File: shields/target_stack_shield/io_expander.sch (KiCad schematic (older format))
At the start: 8 parts

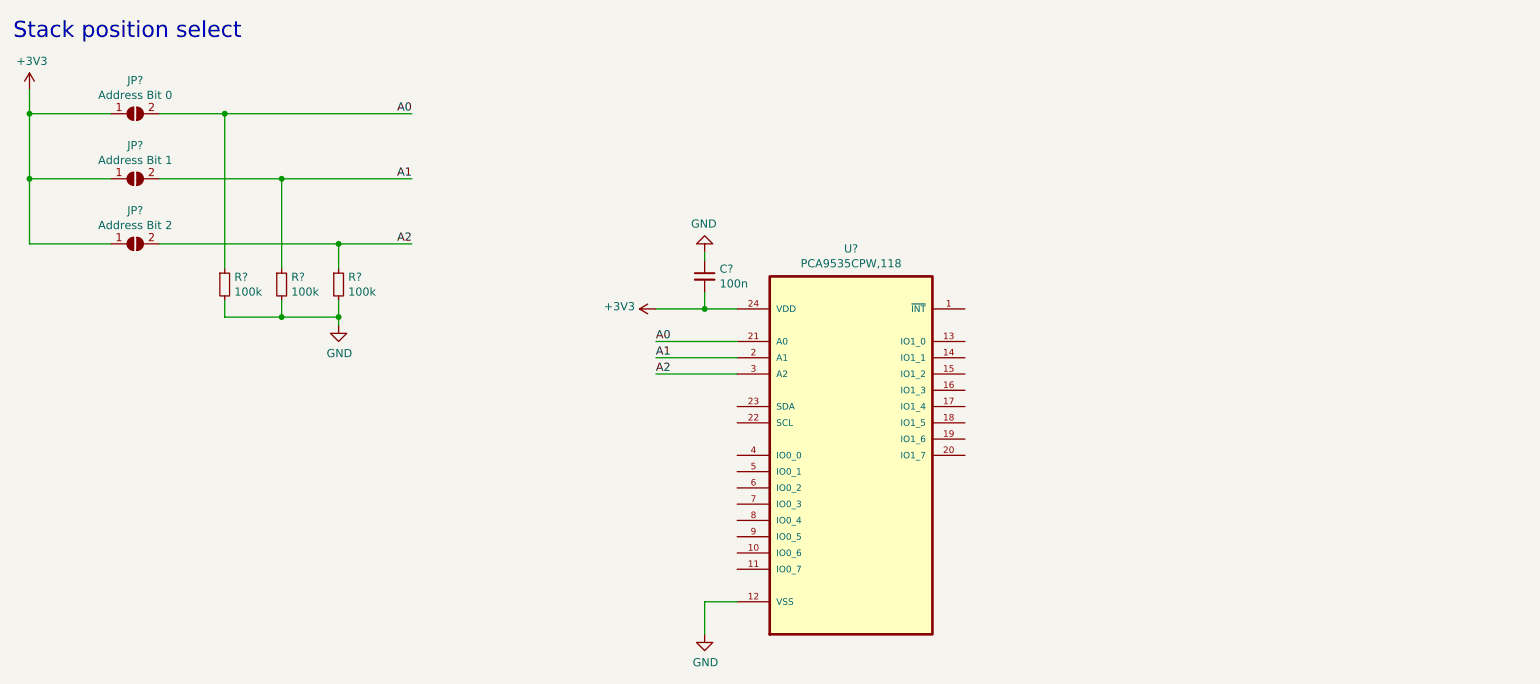
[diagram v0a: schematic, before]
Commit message: further work on target stack shield schematics
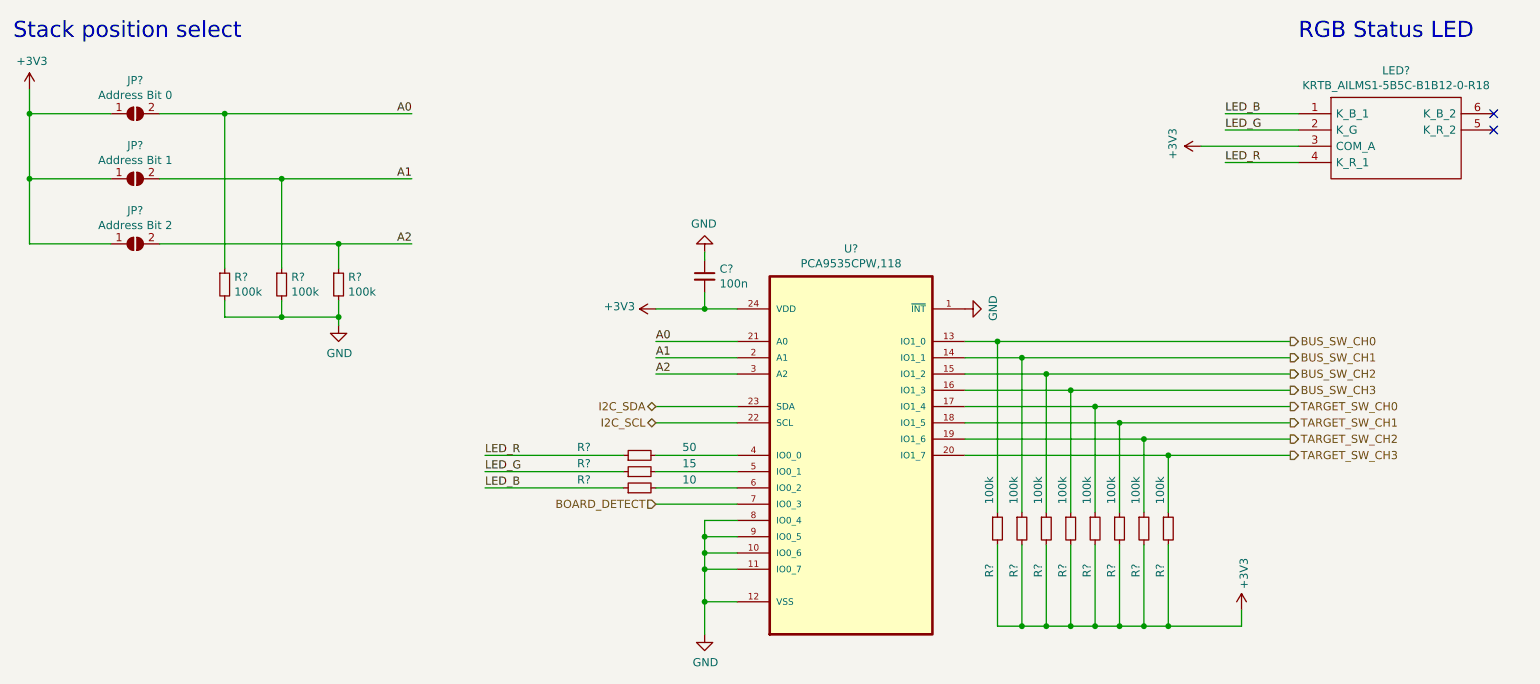
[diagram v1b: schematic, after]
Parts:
- added LED?: KRTB_AILMS1-5B5C-B1B12-0-R18, KRTBAILMS15B5CB1B120R18, symbol hive:KRTB_AILMS1-5B5C-B1B12-0-R18
- added R?: 50, symbol Device:R_Small
- added R?: 15, symbol Device:R_Small
- added R?: 10, symbol Device:R_Small
- added R? (x8): 100k, symbol Device:R_Small
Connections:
- net +3V3: now also LED?.3 (COM_A), R?.2, R?.2, R?.2, R?.2, R?.2, R?.2, R?.2, R?.2
- net GND: now also U?.1 (~INT), U?.10 (IO0_6), U?.11 (IO0_7), U?.8 (IO0_4), U?.9 (IO0_5)
- net BUS_SW_CH0: now reaches U?.13 (IO1_0)
- net BUS_SW_CH0: now also R?.1
- net BUS_SW_CH1: now reaches U?.14 (IO1_1)
- net BUS_SW_CH1: now also R?.1
- net BUS_SW_CH2: now reaches U?.15 (IO1_2)
- net BUS_SW_CH2: now also R?.1
- net BUS_SW_CH3: now reaches U?.16 (IO1_3)
- net BUS_SW_CH3: now also R?.1
- net TARGET_SW_CH0: now reaches U?.17 (IO1_4)
- net TARGET_SW_CH0: now also R?.1
- net TARGET_SW_CH1: now reaches U?.18 (IO1_5)
- net TARGET_SW_CH1: now also R?.1
- net TARGET_SW_CH2: now reaches U?.19 (IO1_6)
- net TARGET_SW_CH2: now also R?.1
- net TARGET_SW_CH3: now reaches U?.20 (IO1_7)
- net TARGET_SW_CH3: now also R?.1
- net I2C_SCL: now reaches U?.22 (SCL)
- net I2C_SDA: now reaches U?.23 (SDA)
- net at U?.4 (IO0_0): now also R?.2
- net at U?.5 (IO0_1): now also R?.2
- net at U?.6 (IO0_2): now also R?.2
- net BOARD_DETECT: now reaches U?.7 (IO0_3)
- new net LED_B: LED?.1 (K_B_1), R?.1
- new net LED_G: LED?.2 (K_G), R?.1
- new net LED_R: LED?.4 (K_R_1), R?.1
- no-connect marks 0 -> 2
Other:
- note added: "RGB Status LED"

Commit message: implemented changes according to feedback, finished target shield schematics
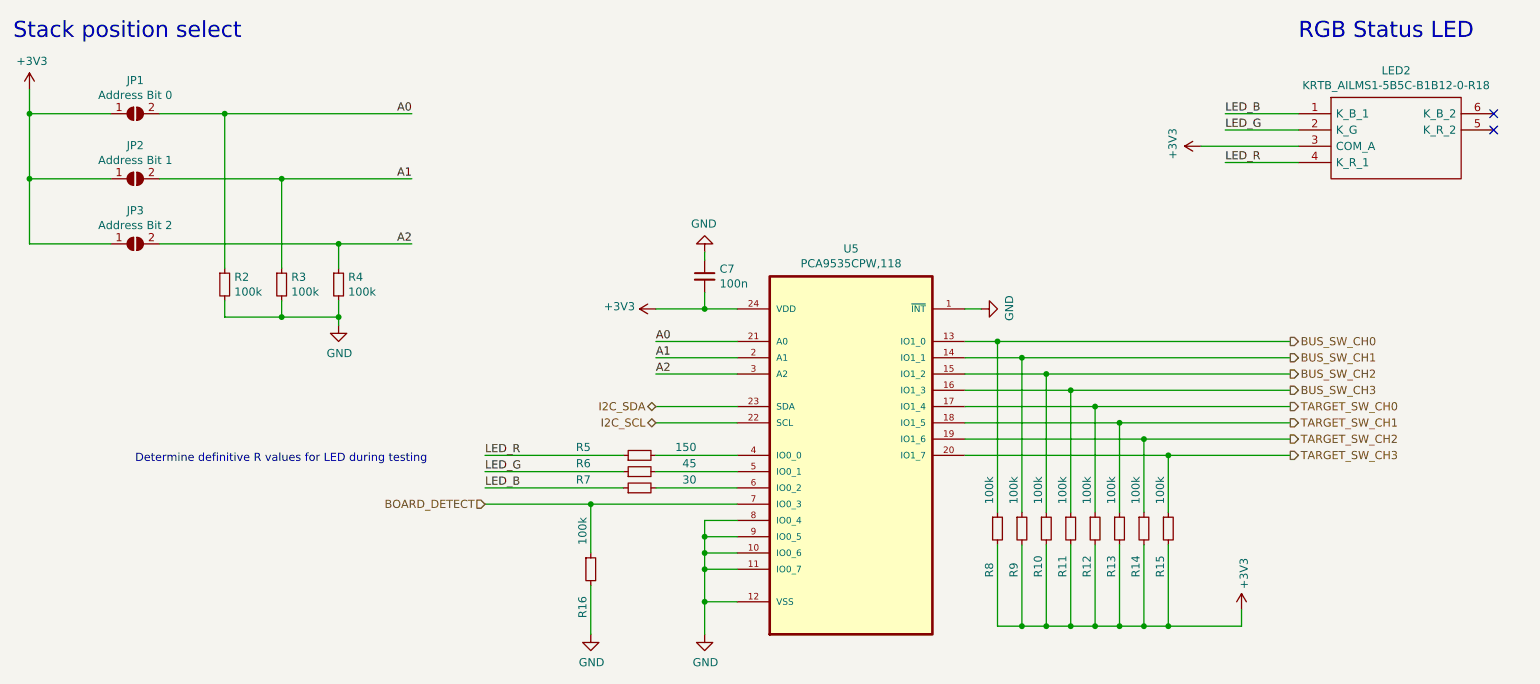
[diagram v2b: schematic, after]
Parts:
- added R16: 100k, symbol Device:R_Small
- R5: renamed from R?; value 50 -> 150
- R6: renamed from R?; value 15 -> 45
- R7: renamed from R?; value 10 -> 30
- gave numbers to parts that had none: 17
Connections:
- net BOARD_DETECT: now also R16.1
- net GND: now also R16.2
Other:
- note added: "Determine definitive R values for LED during testing"
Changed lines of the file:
@@
 $EndDescr
 $Comp
-L hive:PCA9535CPW,118 U?
+L hive:PCA9535CPW,118 U5
 U 1 1 6166B409
 P 6000 3150
-F 0 "U?" H 6000 4320 50  0000 C CNN
+F 0 "U5" H 6000 4320 50  0000 C CNN
 F 1 "PCA9535CPW,118" H 6000 4229 50  0000 C CNN
 F 2 "SOP65P640X110-24N" H 6000 3150 50  0001 L BNN
@@
 $EndComp
 $Comp
-L Jumper:SolderJumper_2_Open JP?
+L Jumper:SolderJumper_2_Open JP1
 U 1 1 6166DA96
 P 1600 1150
-F 0 "JP?" H 1600 1355 50  0000 C CNN
+F 0 "JP1" H 1600 1355 50  0000 C CNN
 F 1 "Address Bit 0" H 1600 1264 50  0000 C CNN
 F 2 "" H 1600 1150 50  0001 C CNN
@@
 $EndComp
 $Comp
-L Jumper:SolderJumper_2_Open JP?
+L Jumper:SolderJumper_2_Open JP2
 U 1 1 6166F0B5
 P 1600 1550
-F 0 "JP?" H 1600 1755 50  0000 C CNN
+F 0 "JP2" H 1600 1755 50  0000 C CNN
 F 1 "Address Bit 1" H 1600 1664 50  0000 C CNN
 F 2 "" H 1600 1550 50  0001 C CNN
@@
 $EndComp
 $Comp
-L Jumper:SolderJumper_2_Open JP?
+L Jumper:SolderJumper_2_Open JP3
 U 1 1 6166F55C
 P 1600 1950
-F 0 "JP?" H 1600 2155 50  0000 C CNN
+F 0 "JP3" H 1600 2155 50  0000 C CNN
 F 1 "Address Bit 2" H 1600 2064 50  0000 C CNN
 F 2 "" H 1600 1950 50  0001 C CNN
@@
 Connection ~ 950  1150
 $Comp
-L power:+3V3 #PWR?
+L power:+3V3 #PWR0143
 U 1 1 6167013E
 P 950 1000
-F 0 "#PWR?" H 950 850 50  0001 C CNN
+F 0 "#PWR0143" H 950 850 50  0001 C CNN
 F 1 "+3V3" H 965 1173 50  0000 C CNN
 F 2 "" H 950 1000 50  0001 C CNN
@@
 	1750 1950 2850 1950
 $Comp
-L Device:R_Small R?
+L Device:R_Small R2
 U 1 1 616716D2
 P 2150 2200
-F 0 "R?" H 2209 2246 50  0000 L CNN
+F 0 "R2" H 2209 2246 50  0000 L CNN
 F 1 "100k" H 2209 2155 50  0000 L CNN
 F 2 "" H 2150 2200 50  0001 C CNN
@@
 $EndComp
 $Comp
-L Device:R_Small R?
+L Device:R_Small R3
 U 1 1 616728EF
 P 2500 2200
-F 0 "R?" H 2559 2246 50  0000 L CNN
+F 0 "R3" H 2559 2246 50  0000 L CNN
 F 1 "100k" H 2559 2155 50  0000 L CNN
 F 2 "" H 2500 2200 50  0001 C CNN
@@
 $EndComp
 $Comp
-L Device:R_Small R?
+L Device:R_Small R4
 U 1 1 61672E4B
 P 2850 2200
-F 0 "R?" H 2909 2246 50  0000 L CNN
+F 0 "R4" H 2909 2246 50  0000 L CNN
 F 1 "100k" H 2909 2155 50  0000 L CNN
 F 2 "" H 2850 2200 50  0001 C CNN
@@
 $EndComp
 $Comp
-L power:GND #PWR?
+L power:GND #PWR0144
 U 1 1 6167330B
 P 2850 2450
-F 0 "#PWR?" H 2850 2200 50  0001 C CNN
+F 0 "#PWR0144" H 2850 2200 50  0001 C CNN
 F 1 "GND" H 2855 2277 50  0000 C CNN
 F 2 "" H 2850 2450 50  0001 C CNN
@@
 A1
 $Comp
-L power:GND #PWR?
+L power:GND #PWR0145
 U 1 1 616781CB
 P 5100 4350
-F 0 "#PWR?" H 5100 4100 50  0001 C CNN
+F 0 "#PWR0145" H 5100 4100 50  0001 C CNN
 F 1 "GND" H 5105 4177 50  0000 C CNN
 F 2 "" H 5100 4350 50  0001 C CNN
@@
 $EndComp
 Wire Wire Line
-	5100 4350 5100 4150
-Wire Wire Line
 	5100 4150 5300 4150
 Wire Wire Line
@@
 	5100 2350 5300 2350
 $Comp
-L Device:C_Small C?
+L Device:C_Small C7
 U 1 1 6167B02A
 P 5100 2150
-F 0 "C?" H 5192 2196 50  0000 L CNN
+F 0 "C7" H 5192 2196 50  0000 L CNN
 F 1 "100n" H 5192 2105 50  0000 L CNN
 F 2 "" H 5100 2150 50  0001 C CNN
@@
 $EndComp
 $Comp
-L power:GND #PWR?
+L power:GND #PWR0146
 U 1 1 6167B936
 P 5100 2000
-F 0 "#PWR?" H 5100 1750 50  0001 C CNN
+F 0 "#PWR0146" H 5100 1750 50  0001 C CNN
 F 1 "GND" H 5105 1827 50  0000 C CNN
 F 2 "" H 5100 2000 50  0001 C CNN
@@
 	5100 2050 5100 2000
 $Comp
-L power:+3V3 #PWR?
+L power:+3V3 #PWR0147
 U 1 1 6167C9DD
 P 4800 2350
-F 0 "#PWR?" H 4800 2200 50  0001 C CNN
+F 0 "#PWR0147" H 4800 2200 50  0001 C CNN
 F 1 "+3V3" V 4815 2478 50  0000 L CNN
 F 2 "" H 4800 2350 50  0001 C CNN
@@
 $EndComp
 $Comp
-L hive:KRTB_AILMS1-5B5C-B1B12-0-R18 LED?
+L hive:KRTB_AILMS1-5B5C-B1B12-0-R18 LED2
 U 1 1 6150EE6A
 P 8750 1150
-F 0 "LED?" H 9350 1415 50  0000 C CNN
+F 0 "LED2" H 9350 1415 50  0000 C CNN
 F 1 "KRTB_AILMS1-5B5C-B1B12-0-R18" H 9350 1324 50  0000 C CNN
 F 2 "KRTBAILMS15B5CB1B120R18" H 9800 1250 50  0001 L CNN
@@
 	8750 1350 8150 1350
 $Comp
-L power:+3V3 #PWR?
+L power:+3V3 #PWR0148
 U 1 1 61513805
 P 8150 1350
-F 0 "#PWR?" H 8150 1200 50  0001 C CNN
+F 0 "#PWR0148" H 8150 1200 50  0001 C CNN
 F 1 "+3V3" H 8165 1523 50  0000 C CNN
 F 2 "" H 8150 1350 50  0001 C CNN
@@
 	5300 3450 4800 3450
 $Comp
-L Device:R_Small R?
+L Device:R_Small R5
 U 1 1 61518C9F
 P 4700 3250
-F 0 "R?" V 4750 3550 50  0000 L CNN
-F 1 "50" V 4750 2900 50  0000 L CNN
+F 0 "R5" V 4750 3550 50  0000 L CNN
+F 1 "150" V 4750 2900 50  0000 L CNN
 F 2 "" H 4700 3250 50  0001 C CNN
 F 3 "~" H 4700 3250 50  0001 C CNN
@@
 $EndComp
 $Comp
-L Device:R_Small R?
+L Device:R_Small R6
 U 1 1 6151A70A
 P 4700 3350
-F 0 "R?" V 4750 3650 50  0000 L CNN
-F 1 "15" V 4750 3000 50  0000 L CNN
+F 0 "R6" V 4750 3650 50  0000 L CNN
+F 1 "45" V 4750 3000 50  0000 L CNN
 F 2 "" H 4700 3350 50  0001 C CNN
 F 3 "~" H 4700 3350 50  0001 C CNN
@@
 $EndComp
 $Comp
-L Device:R_Small R?
+L Device:R_Small R7
 U 1 1 6151A879
 P 4700 3450
-F 0 "R?" V 4750 3750 50  0000 L CNN
-F 1 "10" V 4750 3100 50  0000 L CNN
+F 0 "R7" V 4750 3750 50  0000 L CNN
+F 1 "30" V 4750 3100 50  0000 L CNN
 F 2 "" H 4700 3450 50  0001 C CNN
 F 3 "~" H 4700 3450 50  0001 C CNN
@@
 	6700 3250 7950 3250
 $Comp
-L Device:R_Small R?
+L Device:R_Small R8
 U 1 1 61527FD2
 P 6900 3700
-F 0 "R?" V 6850 3400 50  0000 L CNN
+F 0 "R8" V 6850 3400 50  0000 L CNN
 F 1 "100k" V 6850 3850 50  0000 L CNN
 F 2 "" H 6900 3700 50  0001 C CNN
@@
 $EndComp
 $Comp
-L Device:R_Small R?
+L Device:R_Small R9
 U 1 1 6152ABCB
 P 7050 3700
-F 0 "R?" V 7000 3400 50  0000 L CNN
+F 0 "R9" V 7000 3400 50  0000 L CNN
 F 1 "100k" V 7000 3850 50  0000 L CNN
 F 2 "" H 7050 3700 50  0001 C CNN
@@
 $EndComp
 $Comp
-L Device:R_Small R?
+L Device:R_Small R10
 U 1 1 6152B0EC
 P 7200 3700
-F 0 "R?" V 7150 3400 50  0000 L CNN
+F 0 "R10" V 7150 3400 50  0000 L CNN
 F 1 "100k" V 7150 3850 50  0000 L CNN
 F 2 "" H 7200 3700 50  0001 C CNN
@@
 $EndComp
 $Comp
-L Device:R_Small R?
+L Device:R_Small R11
 U 1 1 6152B483
 P 7350 3700
-F 0 "R?" V 7300 3400 50  0000 L CNN
+F 0 "R11" V 7300 3400 50  0000 L CNN
 F 1 "100k" V 7300 3850 50  0000 L CNN
 F 2 "" H 7350 3700 50  0001 C CNN
@@
 $EndComp
 $Comp
-L Device:R_Small R?
+L Device:R_Small R12
 U 1 1 6152B821
 P 7500 3700
-F 0 "R?" V 7450 3400 50  0000 L CNN
+F 0 "R12" V 7450 3400 50  0000 L CNN
 F 1 "100k" V 7450 3850 50  0000 L CNN
 F 2 "" H 7500 3700 50  0001 C CNN
@@
 $EndComp
 $Comp
-L Device:R_Small R?
+L Device:R_Small R13
 U 1 1 6152BC72
 P 7650 3700
-F 0 "R?" V 7600 3400 50  0000 L CNN
+F 0 "R13" V 7600 3400 50  0000 L CNN
 F 1 "100k" V 7600 3850 50  0000 L CNN
 F 2 "" H 7650 3700 50  0001 C CNN
@@
 $EndComp
 $Comp
-L Device:R_Small R?
+L Device:R_Small R14
 U 1 1 6152C035
 P 7800 3700
-F 0 "R?" V 7750 3400 50  0000 L CNN
+F 0 "R14" V 7750 3400 50  0000 L CNN
 F 1 "100k" V 7750 3850 50  0000 L CNN
 F 2 "" H 7800 3700 50  0001 C CNN
@@
 $EndComp
 $Comp
-L Device:R_Small R?
+L Device:R_Small R15
 U 1 1 6152C503
 P 7950 3700
-F 0 "R?" V 7900 3400 50  0000 L CNN
+F 0 "R15" V 7900 3400 50  0000 L CNN
 F 1 "100k" V 7900 3850 50  0000 L CNN
 F 2 "" H 7950 3700 50  0001 C CNN
@@
 	7050 4300 7200 4300
 $Comp
-L power:+3V3 #PWR?
+L power:+3V3 #PWR0149
 U 1 1 615405C5
 P 8400 4200
-F 0 "#PWR?" H 8400 4050 50  0001 C CNN
+F 0 "#PWR0149" H 8400 4050 50  0001 C CNN
 F 1 "+3V3" V 8415 4328 50  0000 L CNN
 F 2 "" H 8400 4200 50  0001 C CNN
@@
 TARGET_SW_CH3
 Wire Wire Line
-	5300 3550 4800 3550
-Text HLabel 4800 3550 0    50   Input ~ 0
+	5300 3550 4400 3550
+Text HLabel 3750 3550 0    50   Input ~ 0
 BOARD_DETECT
 $Comp
-L power:GND #PWR?
+L power:GND #PWR0150
 U 1 1 6181E123
-P 6700 2350
-F 0 "#PWR?" H 6700 2100 50  0001 C CNN
-F 1 "GND" H 6705 2177 50  0000 C CNN
-F 2 "" H 6700 2350 50  0001 C CNN
-F 3 "" H 6700 2350 50  0001 C CNN
-	1    6700 2350
+P 6800 2350
+F 0 "#PWR0150" H 6800 2100 50  0001 C CNN
+F 1 "GND" H 6805 2177 50  0000 C CNN
+F 2 "" H 6800 2350 50  0001 C CNN
+F 3 "" H 6800 2350 50  0001 C CNN
+	1    6800 2350
 	0    -1   -1   0
 $EndComp
@@
 	5100 3650 5100 3750
 Connection ~ 5100 3750
+Text Notes 1600 3300 0    50   ~ 0
+Determine definitive R values for LED during testing
+Wire Wire Line
+	6700 2350 6800 2350
+$Comp
+L Device:R_Small R16
+U 1 1 62688BC1
+P 4400 3950
+F 0 "R16" V 4350 3650 50  0000 L CNN
+F 1 "100k" V 4350 4100 50  0000 L CNN
+F 2 "" H 4400 3950 50  0001 C CNN
+F 3 "~" H 4400 3950 50  0001 C CNN
+	1    4400 3950
+	1    0    0    -1
+$EndComp
+Wire Wire Line
+	4400 3850 4400 3550
+Connection ~ 4400 3550
+Wire Wire Line
+	4400 3550 3750 3550
+Wire Wire Line
+	5100 4150 5100 4350
+$Comp
+L power:GND #PWR016
+U 1 1 6268E88D
+P 4400 4350
+F 0 "#PWR016" H 4400 4100 50  0001 C CNN
+F 1 "GND" H 4405 4177 50  0000 C CNN
+F 2 "" H 4400 4350 50  0001 C CNN
+F 3 "" H 4400 4350 50  0001 C CNN
+	1    4400 4350
+	1    0    0    -1
+$EndComp
+Wire Wire Line
+	4400 4050 4400 4350
 $EndSCHEMATC
